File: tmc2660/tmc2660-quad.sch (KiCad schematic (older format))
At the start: 0 parts

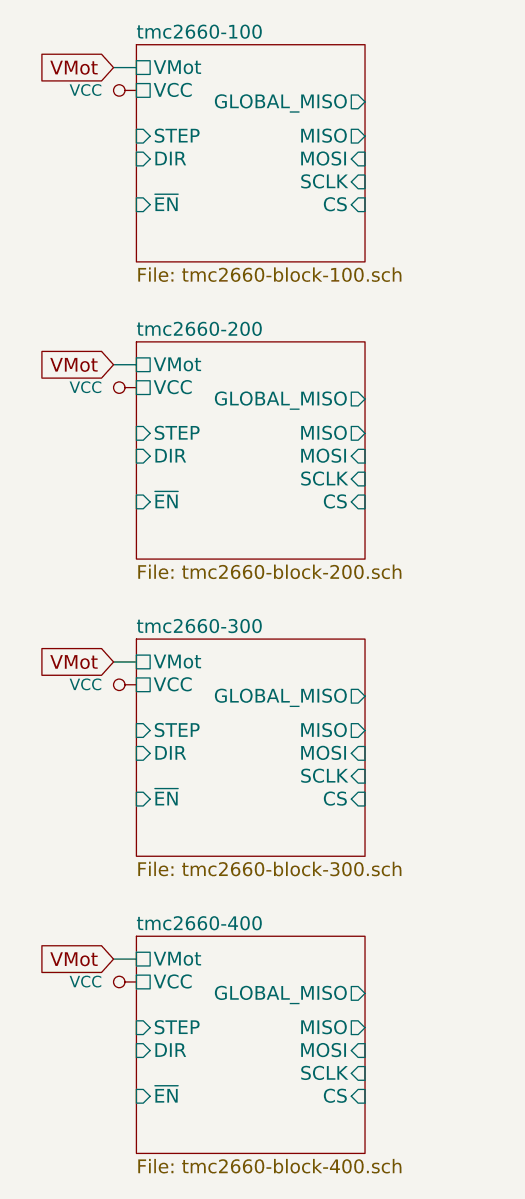
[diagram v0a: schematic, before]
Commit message: Prepare PCB cloning with layout-cloner.
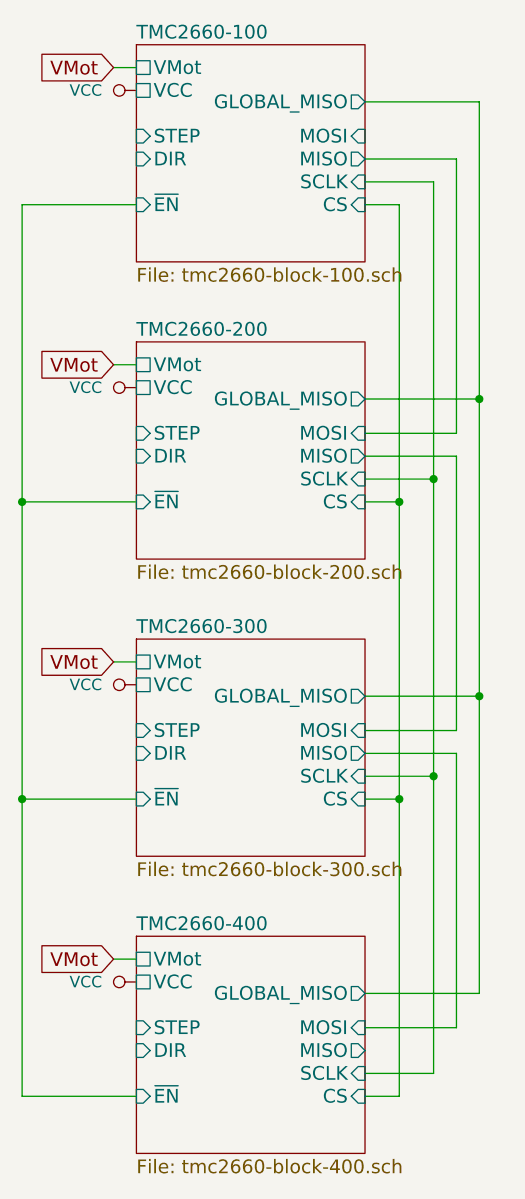
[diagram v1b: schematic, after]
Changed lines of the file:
@@
 EESchema Schematic File Version 4
+LIBS:tmc2660-quad-cache
 EELAYER 26 0
 EELAYER END
 $Descr A4 11693 8268
 encoding utf-8
-Sheet 1 1
+Sheet 1 5
 Title ""
 Date ""
@@
 S 2250 1550 1000 950
 U 5A1094BF
-F0 "tmc2660-100" 60
+F0 "TMC2660-100" 60
 F1 "tmc2660-block-100.sch" 60
-F2 "MISO" O R 3250 1950 60
-F3 "MOSI" I R 3250 2050 60
+F2 "MISO" O R 3250 2050 60
+F3 "MOSI" I R 3250 1950 60
 F4 "SCLK" I R 3250 2150 60
 F5 "CS" I R 3250 2250 60
@@
 S 2250 2850 1000 950
 U 5A109A56
-F0 "tmc2660-200" 60
+F0 "TMC2660-200" 60
 F1 "tmc2660-block-200.sch" 60
-F2 "MISO" O R 3250 3250 60
-F3 "MOSI" I R 3250 3350 60
+F2 "MISO" O R 3250 3350 60
+F3 "MOSI" I R 3250 3250 60
 F4 "SCLK" I R 3250 3450 60
 F5 "CS" I R 3250 3550 60
@@
 S 2250 4150 1000 950
 U 5A10A8D5
-F0 "tmc2660-300" 60
+F0 "TMC2660-300" 60
 F1 "tmc2660-block-300.sch" 60
-F2 "MISO" O R 3250 4550 60
-F3 "MOSI" I R 3250 4650 60
+F2 "MISO" O R 3250 4650 60
+F3 "MOSI" I R 3250 4550 60
 F4 "SCLK" I R 3250 4750 60
 F5 "CS" I R 3250 4850 60
@@
 S 2250 5450 1000 950
 U 5A10AEC6
-F0 "tmc2660-400" 60
+F0 "TMC2660-400" 60
 F1 "tmc2660-block-400.sch" 60
-F2 "MISO" O R 3250 5850 60
-F3 "MOSI" I R 3250 5950 60
+F2 "MISO" O R 3250 5950 60
+F3 "MOSI" I R 3250 5850 60
 F4 "SCLK" I R 3250 6050 60
 F5 "CS" I R 3250 6150 60
@@
 	0    -1   -1   0
 $EndComp
+Wire Wire Line
+	2250 2250 1750 2250
+Wire Wire Line
+	1750 2250 1750 6150
+Wire Wire Line
+	1750 6150 2250 6150
+Wire Wire Line
+	3250 2250 3400 2250
+Wire Wire Line
+	3400 2250 3400 6150
+Wire Wire Line
+	3400 6150 3250 6150
+Wire Wire Line
+	3250 4850 3400 4850
+Connection ~ 3400 4850
+Wire Wire Line
+	3250 3550 3400 3550
+Connection ~ 3400 3550
+Wire Wire Line
+	3250 2150 3550 2150
+Wire Wire Line
+	3550 2150 3550 6050
+Wire Wire Line
+	3550 6050 3250 6050
+Wire Wire Line
+	3250 4750 3550 4750
+Connection ~ 3550 4750
+Wire Wire Line
+	3250 3450 3550 3450
+Connection ~ 3550 3450
+Wire Wire Line
+	3250 2050 3650 2050
+Wire Wire Line
+	3650 2050 3650 3250
+Wire Wire Line
+	3650 3250 3250 3250
+Wire Wire Line
+	3250 3350 3650 3350
+Wire Wire Line
+	3650 3350 3650 4550
+Wire Wire Line
+	3650 4550 3250 4550
+Wire Wire Line
+	3250 4650 3650 4650
+Wire Wire Line
+	3650 4650 3650 5850
+Wire Wire Line
+	3650 5850 3250 5850
+Wire Wire Line
+	3250 5700 3750 5700
+Wire Wire Line
+	3750 5700 3750 1800
+Wire Wire Line
+	3750 1800 3250 1800
+Wire Wire Line
+	3250 3100 3750 3100
+Connection ~ 3750 3100
+Wire Wire Line
+	3250 4400 3750 4400
+Connection ~ 3750 4400
+Wire Wire Line
+	2250 4850 1750 4850
+Connection ~ 1750 4850
+Wire Wire Line
+	2250 3550 1750 3550
+Connection ~ 1750 3550
 $EndSCHEMATC

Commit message: Add connectors.
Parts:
- added J101: Conn_01x04, Connectors_JST:JST_VH_B4PS-VH_2x4x3.96mm_Horizontal, symbol Connector:Conn_01x04
- added J102: Conn_02x08_Odd_Even, Connectors_IDC:IDC-Header_2x08_Pitch2.54mm_Straight, symbol Connector:Conn_02x08_Odd_Even
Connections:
- net labels added: CS, GLOBAL_MISO, GLOBAL_MOSI, GND, SCLK
- wire segments 33 -> 37
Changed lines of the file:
@@
 Text GLabel 2150 1650 0    60   Input ~ 0
 VMot
-Wire Wire Line
-	2150 1650 2250 1650
-$Comp
-L power:VCC #PWR?
+$Comp
+L power:VCC #PWR0111
 U 1 1 5A1094E5
 P 2250 1750
-F 0 "#PWR?" H 2250 1600 50  0001 C CNN
+F 0 "#PWR0111" H 2250 1600 50  0001 C CNN
 F 1 "VCC" V 2250 1900 50  0000 L CNN
 F 2 "" H 2250 1750 50  0001 C CNN
@@
 Text GLabel 2150 2950 0    60   Input ~ 0
 VMot
-Wire Wire Line
-	2150 2950 2250 2950
-$Comp
-L power:VCC #PWR?
+$Comp
+L power:VCC #PWR0112
 U 1 1 5A109A7C
 P 2250 3050
-F 0 "#PWR?" H 2250 2900 50  0001 C CNN
+F 0 "#PWR0112" H 2250 2900 50  0001 C CNN
 F 1 "VCC" V 2250 3200 50  0000 L CNN
 F 2 "" H 2250 3050 50  0001 C CNN
@@
 Text GLabel 2150 4250 0    60   Input ~ 0
 VMot
-Wire Wire Line
-	2150 4250 2250 4250
-$Comp
-L power:VCC #PWR?
+$Comp
+L power:VCC #PWR0113
 U 1 1 5A10A8FB
 P 2250 4350
-F 0 "#PWR?" H 2250 4200 50  0001 C CNN
+F 0 "#PWR0113" H 2250 4200 50  0001 C CNN
 F 1 "VCC" V 2250 4500 50  0000 L CNN
 F 2 "" H 2250 4350 50  0001 C CNN
@@
 Text GLabel 2150 5550 0    60   Input ~ 0
 VMot
-Wire Wire Line
-	2150 5550 2250 5550
-$Comp
-L power:VCC #PWR?
+$Comp
+L power:VCC #PWR0114
 U 1 1 5A10AEEC
 P 2250 5650
-F 0 "#PWR?" H 2250 5500 50  0001 C CNN
+F 0 "#PWR0114" H 2250 5500 50  0001 C CNN
 F 1 "VCC" V 2250 5800 50  0000 L CNN
 F 2 "" H 2250 5650 50  0001 C CNN
@@
 	0    -1   -1   0
 $EndComp
+$Comp
+L Connector:Conn_02x08_Odd_Even J102
+U 1 1 5A1095ED
+P 5250 2850
+F 0 "J102" H 5300 2225 50  0000 C CNN
+F 1 "Conn_02x08_Odd_Even" H 5300 2316 50  0000 C CNN
+F 2 "Connectors_IDC:IDC-Header_2x08_Pitch2.54mm_Straight" H 5250 2850 50  0001 C CNN
+F 3 "~" H 5250 2850 50  0001 C CNN
+	1    5250 2850
+	-1   0    0    1
+$EndComp
+$Comp
+L power:GND #PWR0116
+U 1 1 5A109C26
+P 5450 3150
+F 0 "#PWR0116" H 5450 2900 50  0001 C CNN
+F 1 "GND" V 5455 3022 50  0000 R CNN
+F 2 "" H 5450 3150 50  0001 C CNN
+F 3 "" H 5450 3150 50  0001 C CNN
+	1    5450 3150
+	0    -1   -1   0
+$EndComp
+$Comp
+L power:VCC #PWR0115
+U 1 1 5A109EE9
+P 4950 3150
+F 0 "#PWR0115" H 4950 3000 50  0001 C CNN
+F 1 "VCC" V 4967 3278 50  0000 L CNN
+F 2 "" H 4950 3150 50  0001 C CNN
+F 3 "" H 4950 3150 50  0001 C CNN
+	1    4950 3150
+	0    -1   -1   0
+$EndComp
+Wire Wire Line
+	2150 1650 2250 1650
+Wire Wire Line
+	2150 2950 2250 2950
+Wire Wire Line
+	2150 4250 2250 4250
+Wire Wire Line
+	2150 5550 2250 5550
 Wire Wire Line
 	2250 2250 1750 2250
@@
 	1750 6150 2250 6150
 Wire Wire Line
-	3250 2250 3400 2250
+	3250 2250 3950 2250
 Wire Wire Line
 	3400 2250 3400 6150
@@
 Connection ~ 3400 3550
 Wire Wire Line
-	3250 2150 3550 2150
+	3250 2150 3950 2150
 Wire Wire Line
 	3550 2150 3550 6050
@@
 	3750 5700 3750 1800
 Wire Wire Line
-	3750 1800 3250 1800
+	3250 1800 3950 1800
 Wire Wire Line
 	3250 3100 3750 3100
@@
 	2250 3550 1750 3550
 Connection ~ 1750 3550
+Text GLabel 3950 2250 2    51   Input ~ 0
+CS
+Text GLabel 3950 2150 2    51   Input ~ 0
+SCLK
+Text GLabel 3950 1950 2    51   Input ~ 0
+GLOBAL_MOSI
+Text GLabel 3950 1800 2    51   Output ~ 0
+GLOBAL_MISO
+Connection ~ 3750 1800
+Wire Wire Line
+	3250 1950 3950 1950
+Connection ~ 3550 2150
+Connection ~ 3400 2250
+Text GLabel 5450 3050 2    51   Output ~ 0
+CS
+Text GLabel 4950 3050 0    51   Output ~ 0
+SCLK
+Text GLabel 4950 2950 0    51   Output ~ 0
+GLOBAL_MOSI
+Text GLabel 5450 2950 2    51   Input ~ 0
+GLOBAL_MISO
+$Comp
+L Connector:Conn_01x04 J101
+U 1 1 5A111B0F
+P 900 1800
+F 0 "J101" H 820 1375 50  0000 C CNN
+F 1 "Conn_01x04" H 820 1466 50  0000 C CNN
+F 2 "Connectors_JST:JST_VH_B4PS-VH_2x4x3.96mm_Horizontal" H 900 1800 50  0001 C CNN
+F 3 "~" H 900 1800 50  0001 C CNN
+	1    900  1800
+	-1   0    0    1
+$EndComp
+$Comp
+L power:GND #PWR0110
+U 1 1 5A112185
+P 1100 2000
+F 0 "#PWR0110" H 1100 1750 50  0001 C CNN
+F 1 "GND" H 1105 1827 50  0000 C CNN
+F 2 "" H 1100 2000 50  0001 C CNN
+F 3 "" H 1100 2000 50  0001 C CNN
+	1    1100 2000
+	1    0    0    -1
+$EndComp
+Wire Wire Line
+	1100 1800 1100 2000
+Connection ~ 1100 1900
+Text GLabel 1300 1600 2    60   Output ~ 0
+VMot
+Wire Wire Line
+	1100 1600 1100 1700
+Wire Wire Line
+	1100 1600 1300 1600
+Connection ~ 1100 1600
 $EndSCHEMATC

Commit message: Wire up quad according to new MISO/MOSI sequence.
- Also, add basic STEP/DIR and a capacitor.
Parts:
- added C1: 100u, Capacitors_THT:CP_Radial_D10.0mm_P5.00mm, symbol device:CP
- J1: renamed from J101; value Conn_01x04 -> Power
- J2: renamed from J102; value Conn_02x08_Odd_Even -> DataIn
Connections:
- net labels added: DIR1, DIR2, DIR3, DIR4, MISO, MOSI, STEP1, STEP2, STEP3, STEP4, ~ENABLE
- net labels removed: GLOBAL_MISO, GLOBAL_MOSI
- wire segments 37 -> 61
- no-connect marks 0 -> 1
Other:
- moved on the sheet: J1

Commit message: Initial version of PCB with cloned template components.
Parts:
- removed C1: 100u, Capacitors_THT:CP_Radial_D10.0mm_P5.00mm, symbol device:CP
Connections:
- net labels added: GLOBAL_MISO, GLOBAL_MOSI
- net labels removed: MISO, MOSI
- wire segments 61 -> 47
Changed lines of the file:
@@
 	4350 2250 3850 2250
 Wire Wire Line
-	3850 2250 3850 2700
-Wire Wire Line
-	3850 2700 3850 3550
-Wire Wire Line
-	3850 3550 3850 4850
-Wire Wire Line
-	3850 4850 3850 6150
+	3850 2250 3850 6150
 Wire Wire Line
 	3850 6150 4350 6150
 Wire Wire Line
-	5350 2250 5500 2250
-Wire Wire Line
-	5500 2250 6050 2250
+	5350 2250 6050 2250
 Wire Wire Line
 	5500 6150 5350 6150
@@
 Connection ~ 5500 3550
 Wire Wire Line
-	5350 2150 5650 2150
+	5350 2150 6050 2150
 Wire Wire Line
-	5650 2150 6050 2150
-Wire Wire Line
-	5650 2150 5650 3450
-Wire Wire Line
-	5650 3450 5650 4750
-Wire Wire Line
-	5650 4750 5650 6050
+	5650 2150 5650 6050
 Wire Wire Line
 	5650 6050 5350 6050
@@
 	5350 5700 5850 5700
 Wire Wire Line
-	5850 5700 5850 4400
+	5850 1800 5850 5950
 Wire Wire Line
-	5850 4400 5850 3100
-Wire Wire Line
-	5850 3100 5850 1800
-Wire Wire Line
-	5350 1800 5850 1800
-Wire Wire Line
-	5850 1800 6050 1800
+	5350 1800 6050 1800
 Wire Wire Line
 	5350 3100 5850 3100
@@
 SCLK
 Text GLabel 6050 1950 2    51   Output ~ 0
-MISO
+GLOBAL_MISO
 Text GLabel 6050 1800 2    51   Input ~ 0
-MOSI
+GLOBAL_MOSI
 Connection ~ 5850 1800
 Connection ~ 5650 2150
@@
 SCLK
 Text GLabel 2800 3450 2    51   Output ~ 0
-MOSI
+GLOBAL_MOSI
 Text GLabel 2300 3450 0    51   Input ~ 0
-MISO
+GLOBAL_MISO
 $Comp
 L Connector:Conn_01x04 J1
@@
 $EndComp
 Wire Wire Line
-	2650 1800 2650 1900
-Wire Wire Line
-	2650 1900 2650 2000
+	2650 1800 2650 2000
 Connection ~ 2650 1900
-Text GLabel 3050 1600 2    60   Output ~ 0
+Text GLabel 2900 1600 2    60   Output ~ 0
 VMot
 Wire Wire Line
 	2650 1600 2650 1700
 Wire Wire Line
-	2650 1600 2850 1600
-Wire Wire Line
-	2850 1600 3050 1600
+	2650 1600 2900 1600
 Connection ~ 2650 1600
 Wire Wire Line
-	5500 2250 5500 3550
-Wire Wire Line
-	5500 3550 5500 4850
-Wire Wire Line
-	5500 4850 5500 6150
+	5500 2250 5500 6150
 $Sheet
 S 4350 2850 1000 950
@@
 DIR4
 NoConn ~ 2800 3250
-$Comp
-L device:CP C1
-U 1 1 5A13C16B
-P 2850 1750
-F 0 "C1" H 2850 2000 50  0000 L CNN
-F 1 "100u" H 3050 1750 50  0000 L CNN
-F 2 "Capacitors_THT:CP_Radial_D10.0mm_P5.00mm" H 2888 1600 30  0001 C CNN
-F 3 "" H 2850 1750 60  0000 C CNN
-	1    2850 1750
-	1    0    0    -1
-$EndComp
-Connection ~ 2850 1600
 Wire Wire Line
-	2650 1900 2850 1900
+	5350 5950 5850 5950
+Connection ~ 5850 5700
 $EndSCHEMATC

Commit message: Add leftmost screw holes; Move IDC connector down.
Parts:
- added M0, M1: Mount, Mounting_Holes:MountingHole_2.7mm_M2.5, symbol Mechanical:Mounting_Hole
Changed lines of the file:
@@
 	5350 5950 5850 5950
 Connection ~ 5850 5700
+$Comp
+L Mechanical:Mounting_Hole M0
+U 1 1 5A1112B3
+P 2300 4600
+F 0 "M0" H 2358 4720 50  0000 L CNN
+F 1 "Mount" H 2358 4629 50  0000 L CNN
+F 2 "Mounting_Holes:MountingHole_2.7mm_M2.5" H 2500 4600 50  0001 C CNN
+F 3 "~" H 2500 4600 50  0001 C CNN
+	1    2300 4600
+	1    0    0    -1
+$EndComp
+$Comp
+L Mechanical:Mounting_Hole M1
+U 1 1 5A1112BA
+P 2700 4600
+F 0 "M1" H 2758 4720 50  0000 L CNN
+F 1 "Mount" H 2758 4629 50  0000 L CNN
+F 2 "Mounting_Holes:MountingHole_2.7mm_M2.5" H 2900 4600 50  0001 C CNN
+F 3 "~" H 2900 4600 50  0001 C CNN
+	1    2700 4600
+	1    0    0    -1
+$EndComp
 $EndSCHEMATC

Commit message: Add a fuse.
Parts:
- added F1: Fuse, Fuses:BladeFuse-Mini_Keystone-3586, symbol device:Fuse
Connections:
- net labels added: PowerIn
- wire segments 47 -> 62
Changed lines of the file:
@@
 	4350 2250 3850 2250
 Wire Wire Line
-	3850 2250 3850 6150
+	3850 2250 3850 2700
+Wire Wire Line
+	3850 2700 3850 3550
+Wire Wire Line
+	3850 3550 3850 4850
+Wire Wire Line
+	3850 4850 3850 6150
 Wire Wire Line
 	3850 6150 4350 6150
 Wire Wire Line
-	5350 2250 6050 2250
+	5350 2250 5500 2250
+Wire Wire Line
+	5500 2250 6050 2250
 Wire Wire Line
 	5500 6150 5350 6150
@@
 Connection ~ 5500 3550
 Wire Wire Line
-	5350 2150 6050 2150
-Wire Wire Line
-	5650 2150 5650 6050
+	5350 2150 5650 2150
+Wire Wire Line
+	5650 2150 6050 2150
+Wire Wire Line
+	5650 2150 5650 3450
+Wire Wire Line
+	5650 3450 5650 4750
+Wire Wire Line
+	5650 4750 5650 6050
 Wire Wire Line
 	5650 6050 5350 6050
@@
 	5350 5700 5850 5700
 Wire Wire Line
-	5850 1800 5850 5950
-Wire Wire Line
-	5350 1800 6050 1800
+	5850 1800 5850 3100
+Wire Wire Line
+	5850 3100 5850 4400
+Wire Wire Line
+	5850 4400 5850 5700
+Wire Wire Line
+	5850 5700 5850 5950
+Wire Wire Line
+	5350 1800 5850 1800
+Wire Wire Line
+	5850 1800 6050 1800
 Wire Wire Line
 	5350 3100 5850 3100
@@
 $EndComp
 Wire Wire Line
-	2650 1800 2650 2000
+	2650 1800 2650 1900
+Wire Wire Line
+	2650 1900 2650 2000
 Connection ~ 2650 1900
-Text GLabel 2900 1600 2    60   Output ~ 0
+Text GLabel 3500 1600 2    60   Output ~ 0
 VMot
 Wire Wire Line
 	2650 1600 2650 1700
 Wire Wire Line
-	2650 1600 2900 1600
+	2650 1600 3050 1600
 Connection ~ 2650 1600
 Wire Wire Line
-	5500 2250 5500 6150
+	5500 2250 5500 3550
+Wire Wire Line
+	5500 3550 5500 4850
+Wire Wire Line
+	5500 4850 5500 6150
 $Sheet
 S 4350 2850 1000 950
@@
 	1    0    0    -1
 $EndComp
+$Comp
+L device:Fuse F1
+U 1 1 5A1105FC
+P 3200 1600
+F 0 "F1" V 3003 1600 50  0000 C CNN
+F 1 "Fuse" V 3094 1600 50  0000 C CNN
+F 2 "Fuses:BladeFuse-Mini_Keystone-3586" V 3130 1600 50  0001 C CNN
+F 3 "" H 3200 1600 50  0001 C CNN
+	1    3200 1600
+	0    1    1    0
+$EndComp
+Wire Wire Line
+	3350 1600 3500 1600
+Text Label 2700 1600 0    60   ~ 0
+PowerIn
 $EndSCHEMATC

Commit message: Add digital connector legend. Round board corners.
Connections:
- wire segments 62 -> 48
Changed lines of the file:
@@
 	4350 2250 3850 2250
 Wire Wire Line
-	3850 2250 3850 2700
-Wire Wire Line
-	3850 2700 3850 3550
-Wire Wire Line
-	3850 3550 3850 4850
-Wire Wire Line
-	3850 4850 3850 6150
+	3850 2250 3850 6150
 Wire Wire Line
 	3850 6150 4350 6150
 Wire Wire Line
-	5350 2250 5500 2250
-Wire Wire Line
-	5500 2250 6050 2250
+	5350 2250 6050 2250
 Wire Wire Line
 	5500 6150 5350 6150
@@
 Connection ~ 5500 3550
 Wire Wire Line
-	5350 2150 5650 2150
+	5350 2150 6050 2150
 Wire Wire Line
-	5650 2150 6050 2150
-Wire Wire Line
-	5650 2150 5650 3450
-Wire Wire Line
-	5650 3450 5650 4750
-Wire Wire Line
-	5650 4750 5650 6050
+	5650 2150 5650 6050
 Wire Wire Line
 	5650 6050 5350 6050
@@
 	5350 5700 5850 5700
 Wire Wire Line
-	5850 1800 5850 3100
+	5850 1800 5850 5950
 Wire Wire Line
-	5850 3100 5850 4400
-Wire Wire Line
-	5850 4400 5850 5700
-Wire Wire Line
-	5850 5700 5850 5950
-Wire Wire Line
-	5350 1800 5850 1800
-Wire Wire Line
-	5850 1800 6050 1800
+	5350 1800 6050 1800
 Wire Wire Line
 	5350 3100 5850 3100
@@
 $EndComp
 Wire Wire Line
-	2650 1800 2650 1900
-Wire Wire Line
-	2650 1900 2650 2000
+	2650 1800 2650 2000
 Connection ~ 2650 1900
 Text GLabel 3500 1600 2    60   Output ~ 0
@@
 Connection ~ 2650 1600
 Wire Wire Line
-	5500 2250 5500 3550
-Wire Wire Line
-	5500 3550 5500 4850
-Wire Wire Line
-	5500 4850 5500 6150
+	5500 2250 5500 6150
 $Sheet
 S 4350 2850 1000 950

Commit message: Rename local *.pretty to project name.
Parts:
- F1: footprint Fuses:BladeFuse-Mini_Keystone-3586 -> Quadrigotion:BladeFuse-Mini_Keystone-3586
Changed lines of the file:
@@
 F 0 "F1" V 3003 1600 50  0000 C CNN
 F 1 "Fuse" V 3094 1600 50  0000 C CNN
-F 2 "Fuses:BladeFuse-Mini_Keystone-3586" V 3130 1600 50  0001 C CNN
+F 2 "Quadrigotion:BladeFuse-Mini_Keystone-3586" V 3130 1600 50  0001 C CNN
 F 3 "" H 3200 1600 50  0001 C CNN
 	1    3200 1600
